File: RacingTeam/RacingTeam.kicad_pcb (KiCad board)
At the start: 4 copper layers, 122.5 x 92.5 mm, 81 parts, among them J1 BusIn, J10 BatteryIn, J11 ShutdownIn, J2 Conn_01x01, J3 Conn_01x01, J4 Conn_01x01, J5 Conn_01x01, J6 PreCharge Relay Out, J7 AIROut, J8 Discharge Relay Out, J9 PCB OUT, Q1 TP0610T, Q2 2N7002, Q3 2N7002, Q4 2N7002, Q5 2N7002, Q6 TP0610T, Q7 2N7002, Q8 TP0610T, U1 LM311, U2 LM311, U3 4N35, U6 NE555D

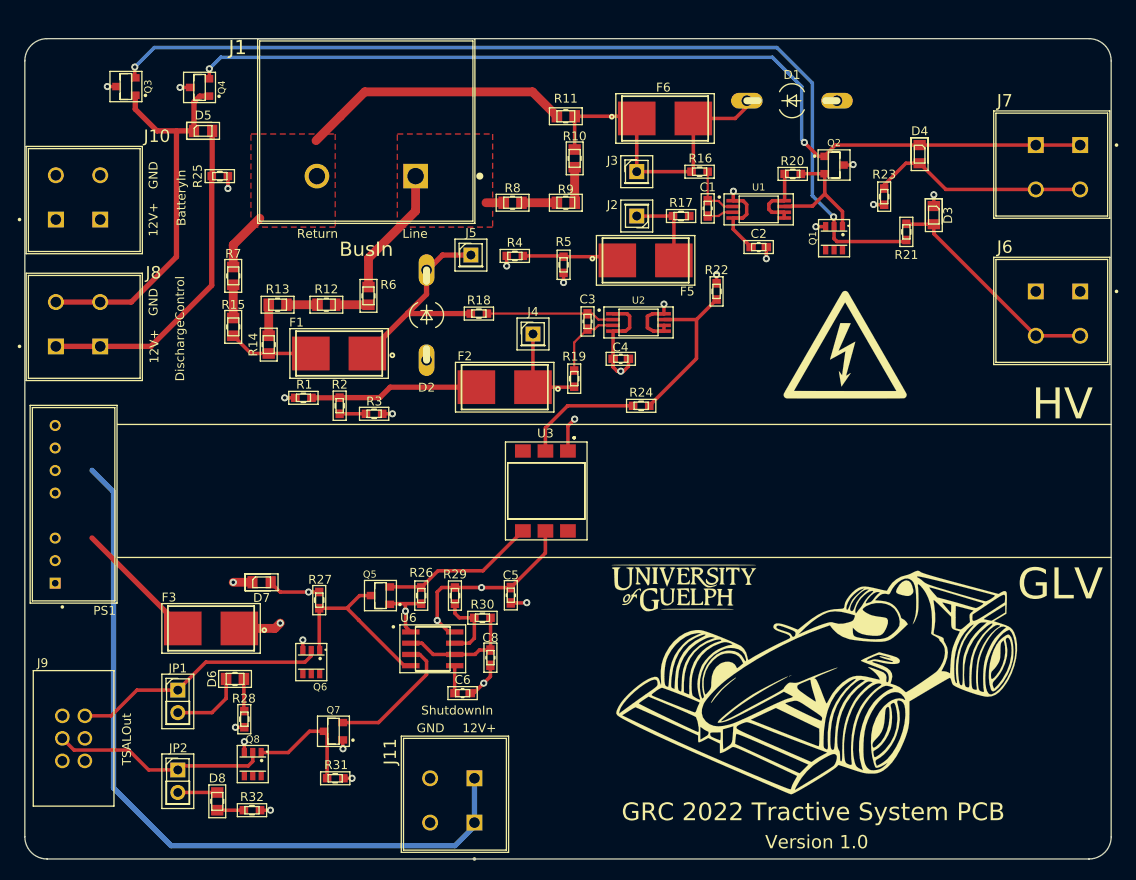
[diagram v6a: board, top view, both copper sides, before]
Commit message: Update 2N7002H6327XTSA2.kicad_mod, 4N35SM.kicad_mod, and 69 more files...
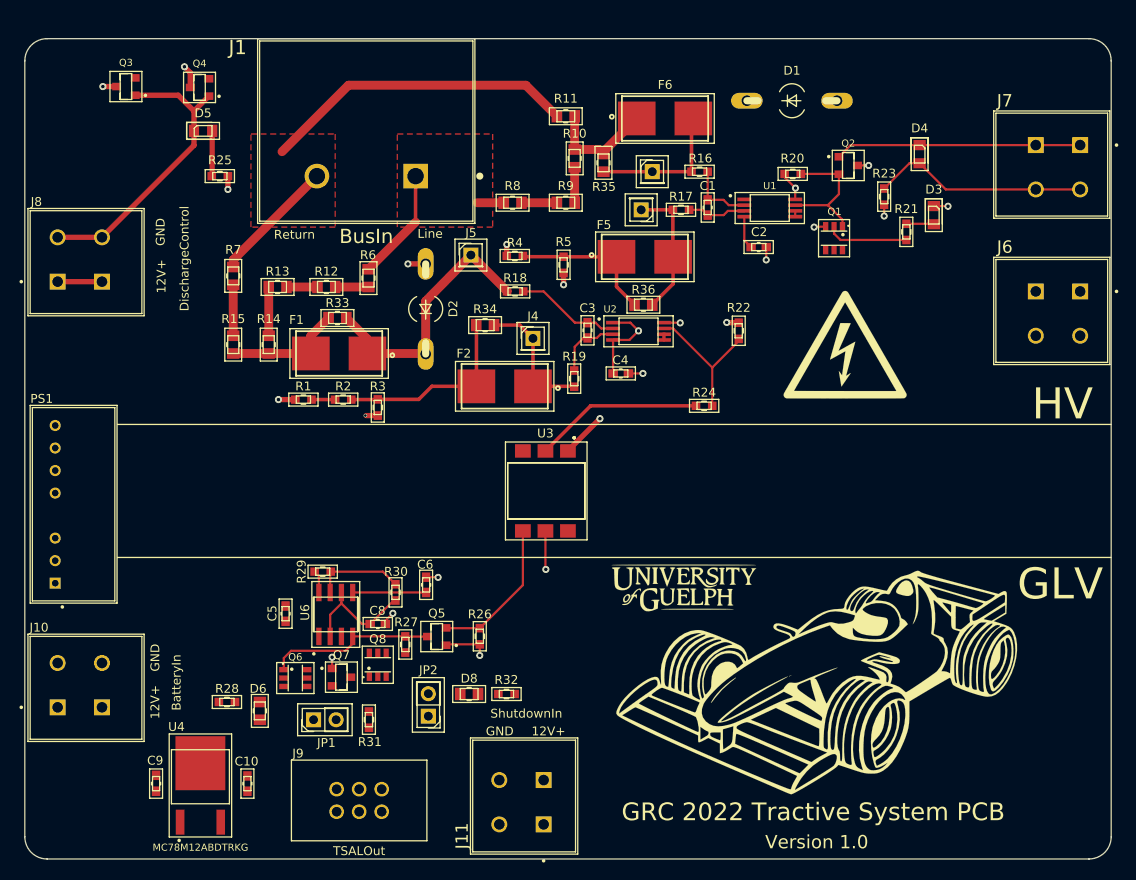
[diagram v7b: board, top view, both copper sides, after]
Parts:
- removed D7: D, GRC2022:SD0805S040S0R5
- removed F3: Fuse_Small, GRC2022:FUSE_0154004.DRTL
- added C10: 1μF, GRC2022:C_0603, F.Cu at (134.6, 115.0)
- added C9: 1μF, GRC2022:C_0603, F.Cu at (124.3, 115.0)
- added R33: 0Ω, GRC2022:R_0805, F.Cu at (144.8, 62.5)
- added R34: 0Ω, GRC2022:R_0805, F.Cu at (161.4, 63.3)
- added R35: 0Ω, GRC2022:R_0805, F.Cu at (174.8, 45.0)
- added R36: 0Ω, GRC2022:R_0805, F.Cu at (179.2, 61.0)
- added U4: MC78M12ABDTRKG, GRC2022:TO229P990X238-4N, F.Cu at (129.3, 115.2)
- J2: value Conn_01x01 -> Bypass Pin
- J3, J4, J5: value Conn_01x01 -> BypassPin
- J9: value PCB OUT -> Deutsch DTM
- R10, R8, R9: value 150kOhm -> 150kΩ
- R11: value 4kOhm -> 4kΩ
- R20, R22: value 22kΩ -> 20kΩ
- moved J10 55.0 mm to (113.2, 106.4)
- moved J9 33.0 mm to (147.2, 116.9), turned to 0 degrees
- moved R32 31.5 mm to (163.8, 104.9), turned to 180 degrees
- moved D8 30.9 mm to (159.6, 104.9), turned to 180 degrees
- moved JP2 28.9 mm to (155.0, 107.4), turned to 180 degrees
- moved C5 25.5 mm to (138.9, 95.8)
- moved Q8 18.0 mm to (149.3, 101.6), turned to 90 degrees
- moved JP1 15.7 mm to (142.1, 107.8), turned to 90 degrees
- moved R29 15.2 mm to (143.1, 91.1), turned to 0 degrees
- moved C8 13.3 mm to (149.3, 97.0), turned to 0 degrees
- moved C6 12.9 mm to (154.8, 92.6), turned to 90 degrees
- moved U6 11.6 mm to (144.6, 95.9), turned to 90 degrees
- moved R27 10.9 mm to (152.4, 99.3), turned to 90 degrees
- moved R30 10.2 mm to (151.3, 93.4), turned to 270 degrees
- moved R26 8.04 mm to (160.8, 98.4)
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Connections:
- net /555DischargePullup renamed /555Discharge
- net /555Drive renamed /555DriveRED
- net /555Ouput renamed /555Output
- net /CompOut renamed /TSALCompOut
- net /LM311V+ renamed /TSAL_LM311V+
- net /LM311V- renamed /TSAL_LM311V-
- net /PrechargeOUT renamed /PrechargeCompOUT
- net /TSALBus renamed /BusRefTSAL
- net AIROn renamed /AIRON
- net BusLine renamed /BusLine
- net BusReturn renamed /BusReturn
- net RED+ renamed /RED+
- net Shutdown+ renamed /Shutdown
- C5 pad 1: VCC -> GLV+
- C5 pad 2: GLV- -> -BATT
- C6 pad 2: GLV- -> -BATT
- C8 pad 2: GLV- -> -BATT
- D1 pad 1: /PrechargeRef1 -> /PrechargeBus
- F1 pad 2: /TSALRef -> /BusOutTSAL
- F2 pad 1: /TSALCommon -> /TSALRef
- F2 pad 2: /TSALREF -> /TSALREFOut
- F6 pad 1: /PrechargeRef1 -> /PrechargeBus
- F6 pad 2: /PrechargeRef1 -> /PrechargeTP+
- J10 pad 1: +12V -> +BATT
- J10 pad 2: GND -> -BATT
- J11 pad 2: GLV- -> -BATT
- J3 pad 1: /PrechargeRef1 -> /PrechargeTP+
- J4 pad 1: /TSALCommon -> /TSALRef
- J9 pad 2: Green+ -> /Green+
- J9 pad 4: GLV- -> -BATT
- J9 pad 5: GLV- -> -BATT
- J9 pad 6: GLV- -> -BATT
- JP1 pad 1: Green+ -> /OBLEDGreen
- JP1 pad 2: /OBLEDGreen -> /Green+
- PS1 pad 1: GND -> -BATT
- PS1 pad 2: +12V -> +BATT
- PS1 pad 6: /Ec3Out+ -> +12V
- PS1 pad 7: GLV- -> GND
- Q1 pad 2: PreChargeOn -> Net-(Q1-Pad2)
- Q3 pad 2: PreChargeOn -> GND
- Q5 pad 1: GLV- -> -BATT
- Q6 pad 2: Green+ -> /Green+
- Q7 pad 1: GLV- -> -BATT
- R1 pad 1: /TSALREF -> Net-(R1-Pad1)
- R10 pad 2: /PrechargeRef1 -> /PrechargeBus
- R11 pad 1: /PrechargeRef1 -> /PrechargeBus
- R14 pad 2: /TSALRef -> /BusOutTSAL
- R15 pad 1: /TSALRef -> /BusOutTSAL
- R16 pad 2: /PrechargeRef1 -> /PrechargeTP+
- R19 pad 2: /TSALCommon -> /TSALRef
- R2 pad 1: Net-(R2-Pad1) -> /TSALREFOut
- R2 pad 2: /TSALREF -> Net-(R1-Pad1)
- R20 pad 2: /PreChargePullup -> +12V
- R21 pad 1: PreChargeOn -> Net-(Q1-Pad2)
- R26 pad 2: GLV- -> -BATT
- R27 pad 1: VCC -> GLV+
- R28 pad 2: GLV- -> -BATT
- R29 pad 1: VCC -> GLV+
- R3 pad 2: Net-(R2-Pad1) -> /TSALREFOut
- R32 pad 2: GLV- -> -BATT
- U1 pad 5: /PreChargePullup -> Net-(U1-Pad5)
- U1 pad 6: /PreChargePullup -> Net-(U1-Pad5)
- U1 pad 8: /PreChargePullup -> +12V
- U2 pad 5: +12V -> Net-(U2-Pad5)
- U2 pad 6: +12V -> Net-(U2-Pad5)
- U3 pad 5: VCC -> GLV+
- U6 pad 1: GLV- -> -BATT
- U6 pad 8: VCC -> GLV+
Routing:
- net PreChargeOn: track 107.1 -> 0.00 mm, vias 2 -> 0
- net /Shutdown: track 86.5 -> 0.00 mm
- net /AIRON: track 108.6 -> 27.7 mm, vias 2 -> 0
- net /PrechargeRef1: track 36.1 -> 0.00 mm
- net VCC: track 33.1 -> 0.00 mm, vias 4 -> 0
- net Green+: track 28.9 -> 0.00 mm
- net /DischargeOut: track 37.9 -> 10.1 mm
- net /RED+: track 24.3 -> 0.00 mm
- net /PrechargeRelayOut: track 25.5 -> 3.12 mm
- net /TSALREFOut: track 0.00 -> 21.6 mm
- net /TSALREF: track 19.1 -> 0.00 mm
- net GLV-: track 16.3 -> 0.00 mm, vias 6 -> 0
- net /PrechargeTP+: track 0.00 -> 16.0 mm
- net /555Output: track 15.3 -> 0.00 mm
- net /Ec3Out+: track 14.5 -> 0.00 mm
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- added copper zone on GND, net -BATT
- removed copper zone on GND, net GLV-
- removed copper zone on PWR, net VCC
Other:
- net class Large: clearance 0.4 -> 0.2
- net class Small: clearance 0.1 -> 0.2; via_dia 0.8 -> 0.4; via_drill 0.4 -> 0.3

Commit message: Update GRC22Footprints.mod, C_0603_1608Metric.step, and 19 more files...
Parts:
- added Q4: TP0610T, GRC22Footprints:2N7002H6327XTSA2_v2, F.Cu at (118.2, 40.7)
- C1, C10, C2, C3, C4, C5, C6, C8, C9: footprint GRC2022:C_0603 -> GRC22Footprints:C_0603_1608Metric_Pad1.08x0.95mm_HandSolder
- D1, D2: footprint GRC2022:SOD57-10 -> GRC22Footprints:SOD57-10
- D3, D4, D5: footprint GRC2022:SD0805S040S0R5 -> GRC22Footprints:D_0805_2012Metric_Castellated
- D6, D8: footprint GRC2022:SunLED -> GRC22Footprints:D_0603_1608Metric_Castellated
- F1, F2, F5, F6: footprint GRC2022:FUSE_0154004.DRTL -> GRC22Footprints:FUSE_0154004.DRTL
- J1: footprint GRC2022:TE_8PCV-02-006 -> GRC22Footprints:TE_8PCV-02-006
- J10, J11, J7, J8: footprint GRC2022:CUI_TBL001-500-02GY-2GY -> GRC22Footprints:CUI_TBL001-500-02GY-2GY
- J2, J3, J4, J5: footprint GRC2022:SinglePinHeader -> GRC22Footprints:PinHeader_1x01_P2.54mm_Vertical
- J6: value PreCharge Relay Out -> PC Relay; footprint GRC2022:CUI_TBL001-500-02GY-2GY -> GRC22Footprints:CUI_TBL001-500-02GY-2GY
- J9: value Deutsch DTM -> Molex; footprint GRC2022:Molex -> GRC22Footprints:Molex
- JP1, JP2: footprint GRC2022:DualPinHeader -> GRC22Footprints:PinHeader_1x02_P2.54mm_Vertical
- PS1: footprint GRC2022:EC3SAW-24S12P -> GRC22Footprints:EC3SAW-24S12P
- Q1, Q6, Q8: footprint GRC2022:SOT95P280X100-6N -> GRC22Footprints:2N7002H6327XTSA2_v2
- Q2, Q3, Q5, Q7: footprint GRC2022:TRANS_MMBT2907A -> GRC22Footprints:2N7002H6327XTSA2
- R1, R16, R17, R18, R19, R2, R20, R22, R24, R26, R27, R28, R29, R3, R30, R31, R32, R4, R5: footprint GRC2022:R_0603 -> GRC22Footprints:R_0603_1608Metric_Pad0.98x0.95mm_HandSolder
- R10, R11, R12, R13, R14, R15, R33, R34, R35, R36, R6, R7, R8, R9: footprint GRC2022:R_0805 -> GRC22Footprints:R_0805_2012Metric_Pad1.20x1.40mm_HandSolder
- R21, R23, R25: footprint GRC2022:R_0603 -> GRC22Footprints:R_0805_2012Metric_Pad1.20x1.40mm_HandSolder
- U1, U2: footprint GRC2022:SOP65P640X120-8N -> GRC22Footprints:LM311PW
- U3: footprint GRC2022:OPTO_4N35SM -> GRC22Footprints:OPTO_4N35SM
- U4: footprint GRC2022:TO229P990X238-4N -> GRC22Footprints:TO229P990X238-4N
- U6: footprint GRC2022:NE555PSRE4 -> GRC22Footprints:NE555PSRE4
- moved Q6 16.4 mm to (155.8, 98.5)
- moved C6 14.3 mm to (140.5, 92.9)
- moved R30 14.2 mm to (137.3, 95.9), turned to 90 degrees
- moved C8 13.8 mm to (136.4, 92.0), turned to 180 degrees
- moved R29 10.4 mm to (137.3, 99.7), turned to 90 degrees
- moved C5 8.44 mm to (146.4, 99.7), turned to 0 degrees
- moved Q4 8.02 mm to (124.0, 42.6)
- moved Q8 7.76 mm to (148.3, 109.3), turned to 0 degrees
- moved R35 6.99 mm to (181.7, 45.7), turned to 180 degrees
- moved R26 6.70 mm to (165.6, 93.7)
- moved D3 6.36 mm to (207.4, 55.3)
- moved R27 6.12 mm to (152.7, 93.2), turned to 270 degrees
- moved R21 6.03 mm to (208.4, 58.8), turned to 180 degrees
- moved Q5 6.02 mm to (159.8, 93.8), turned to 0 degrees
- moved R31 5.58 mm to (149.5, 102.3), turned to 270 degrees
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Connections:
- C10 pad 2: -BATT -> GLV-
- C5 pad 2: -BATT -> GLV-
- C6 pad 2: -BATT -> GLV-
- C8 pad 2: -BATT -> GLV-
- C9 pad 2: -BATT -> GLV-
- D3 pad 1: +12V -> /PreChargeON
- D4 pad 1: /AIRON -> +12V
- D4 pad 2: /AIROut -> /AIRON
- J10 pad 2: -BATT -> GLV-
- J11 pad 2: -BATT -> GLV-
- J6 pad 1: +12V -> /PreChargeON
- J7 pad 1: /AIRON -> +12V
- J7 pad 2: /AIROut -> /AIRON
- J9 pad 3: /RED+ -> GLV-
- J9 pad 4: -BATT -> /RED+
- J9 pad 5: -BATT -> GLV-
- J9 pad 6: -BATT -> GLV-
- PS1 pad 1: -BATT -> GLV-
- Q1 pad 2: Net-(Q1-Pad2) -> +12V
- Q1 pad 3: GND -> /PreChargeON
- Q2 pad 1: /AIRON -> /PrechargeCompOUT
- Q2 pad 2: /PrechargeCompOUT -> Net-(Q2-Pad2)
- Q2 pad 3: +12V -> /AIRON
- Q3 pad 1: /DischargeIn -> /PreChargeON
- Q3 pad 2: GND -> /DischargeIn
- Q5 pad 1: -BATT -> Net-(Q5-Pad1)
- Q5 pad 2: /InvertBus -> GLV-
- Q6 pad 2: /Green+ -> GLV+
- Q6 pad 3: GLV+ -> /Green+
- Q7 pad 1: -BATT -> /555Output
- Q7 pad 2: /555Output -> GLV-
- Q8 pad 2: /RED+ -> GLV+
- Q8 pad 3: GLV+ -> /RED+
- R21 pad 1: Net-(Q1-Pad2) -> GND
- R23 pad 2: /AIROut -> Net-(Q2-Pad2)
- R26 pad 1: /InvertBus -> Net-(Q5-Pad1)
- R26 pad 2: -BATT -> GLV-
- R28 pad 2: -BATT -> GLV-
- R32 pad 2: -BATT -> GLV-
- U3 pad 3: Net-(U3-Pad3) -> (no net)
- U3 pad 4: /InvertBus -> Net-(Q5-Pad1)
- U4 pad 4: -BATT -> GLV-
- U6 pad 1: -BATT -> GLV-
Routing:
- net /PreChargeON: track 0.00 -> 134.6 mm, vias 0 -> 2
- net /AIRON: track 27.7 -> 120.0 mm, vias 0 -> 2
- net /Shutdown: track 0.00 -> 79.9 mm
- net GLV-: track 0.00 -> 39.4 mm, vias 0 -> 7
- net /Green+: track 0.00 -> 32.6 mm, vias 0 -> 1
- net +12V: track 22.4 -> 47.6 mm
- net /AIROut: track 24.5 -> 0.00 mm
- net +BATT: track 0.00 -> 24.2 mm
- net /PrechargeRelayOut: track 3.12 -> 27.1 mm
- net /PrechargeBus: track 12.8 -> 32.1 mm
- net /DischargeOut: track 10.1 -> 28.3 mm
- net /InvertBus: track 16.8 -> 0.00 mm
- net GLV+: track 6.92 -> 20.9 mm, vias 1 -> 6
- net /555Output: track 0.00 -> 13.9 mm
- net Net-(Q5-Pad1): track 0.00 -> 13.2 mm
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- added copper zone on F.Cu, net /555Reset
- added copper zone on F.Cu, net /DischargeIn
- added copper zone on GND, net GLV-
- removed copper zone on GND, net -BATT
